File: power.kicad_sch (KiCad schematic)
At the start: 16 parts, among them Q5 AO3401A, SW2 SW_On_Off, U6 TPS61200DRC, U9 MCP73831-2-MC

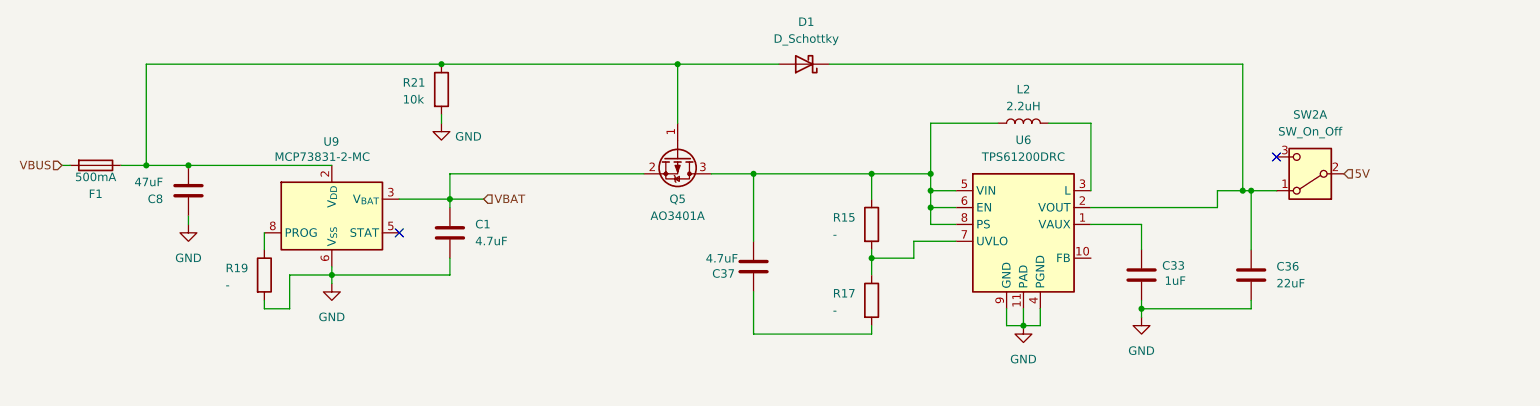
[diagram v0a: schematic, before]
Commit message: finished power circuit
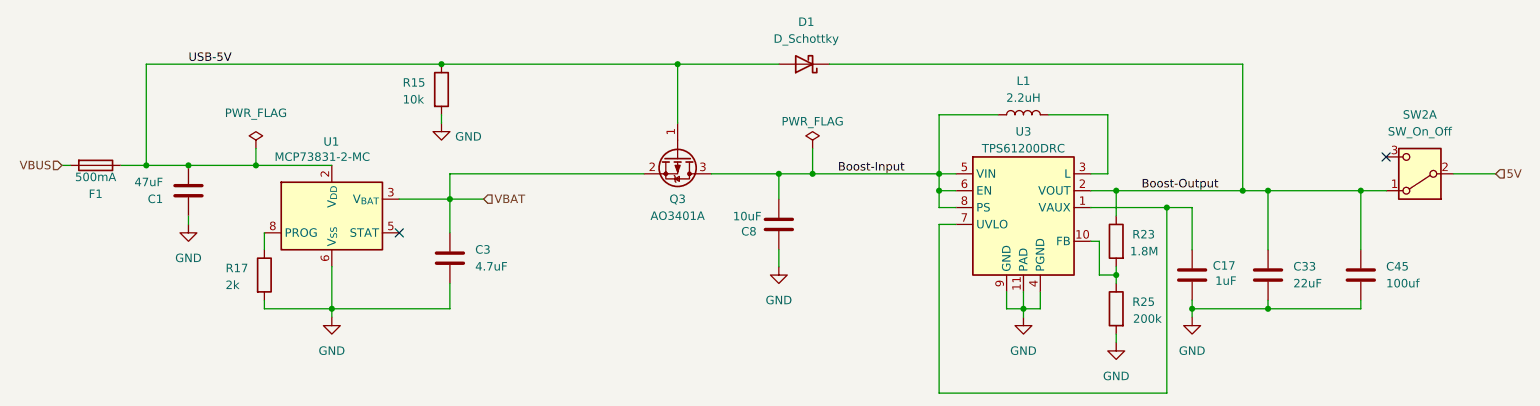
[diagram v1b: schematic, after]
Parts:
- removed R15, R17: -, Resistor_SMD:R_0402_1005Metric, symbol Device:R
- added C45: 100uf, Capacitor_SMD:C_0805_2012Metric, symbol Device:C
- added R23: 1.8M, Resistor_SMD:R_0402_1005Metric, symbol Device:R
- added R25: 200k, Resistor_SMD:R_0402_1005Metric, symbol Device:R
- C1: renamed from C8; footprint Capacitor_SMD:C_0805_2012Metric -> Capacitor_SMD:C_0603_1608Metric
- C3: renamed from C1; footprint Capacitor_SMD:C_0805_2012Metric -> Capacitor_SMD:C_0603_1608Metric
- C33: renamed from C36; footprint (none) -> Capacitor_SMD:C_0603_1608Metric
- C8: renamed from C37; value 4.7uF -> 10uF
- L1: renamed from L2; footprint (none) -> LPS3015-222MRC:IND_LPS3015-222MRC; LCSC (none) -> C2844756
- R17: renamed from R19; value - -> 2k
- U3: renamed from U6; LCSC (none) -> C140320
- renumbered C33 to C17, Q5 to Q3, R21 to R15, U9 to U1
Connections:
- net GND: now also C8.1, C45.1, R25.2
- net Boost-Output: now reaches C33.1, D1.1 (K), SW2.1 (A), U3.2 (VOUT)
- net Boost-Output: now also C45.2, R23.1
- net USB-5V: now reaches C1.2, D1.2 (A), F1.1, Q3.1 (G), R15.1, U1.1 (V_{DD}), U1.2 (V_{DD})
- net Boost-Input: now reaches C8.2, L1.1, Q3.3 (D), U3.5 (VIN), U3.6 (EN), U3.8 (PS)
- net at U3.7 (UVLO): now also C17.1, U3.1 (VAUX)
- net at U3.10 (FB): now also R23.2, R25.1
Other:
- moved on the sheet: C17, C3, C33, C8, L1, SW2A, U3
